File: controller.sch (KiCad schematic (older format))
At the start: 18 parts, among them P1 CONN_2, P2 CONN_2, P3 CONN_2, Q1 Q_NPN_EBC, SW1 SWITCH_INV, U1 LTC6992_TSOT_32_6, U2 POLOLU_3V3

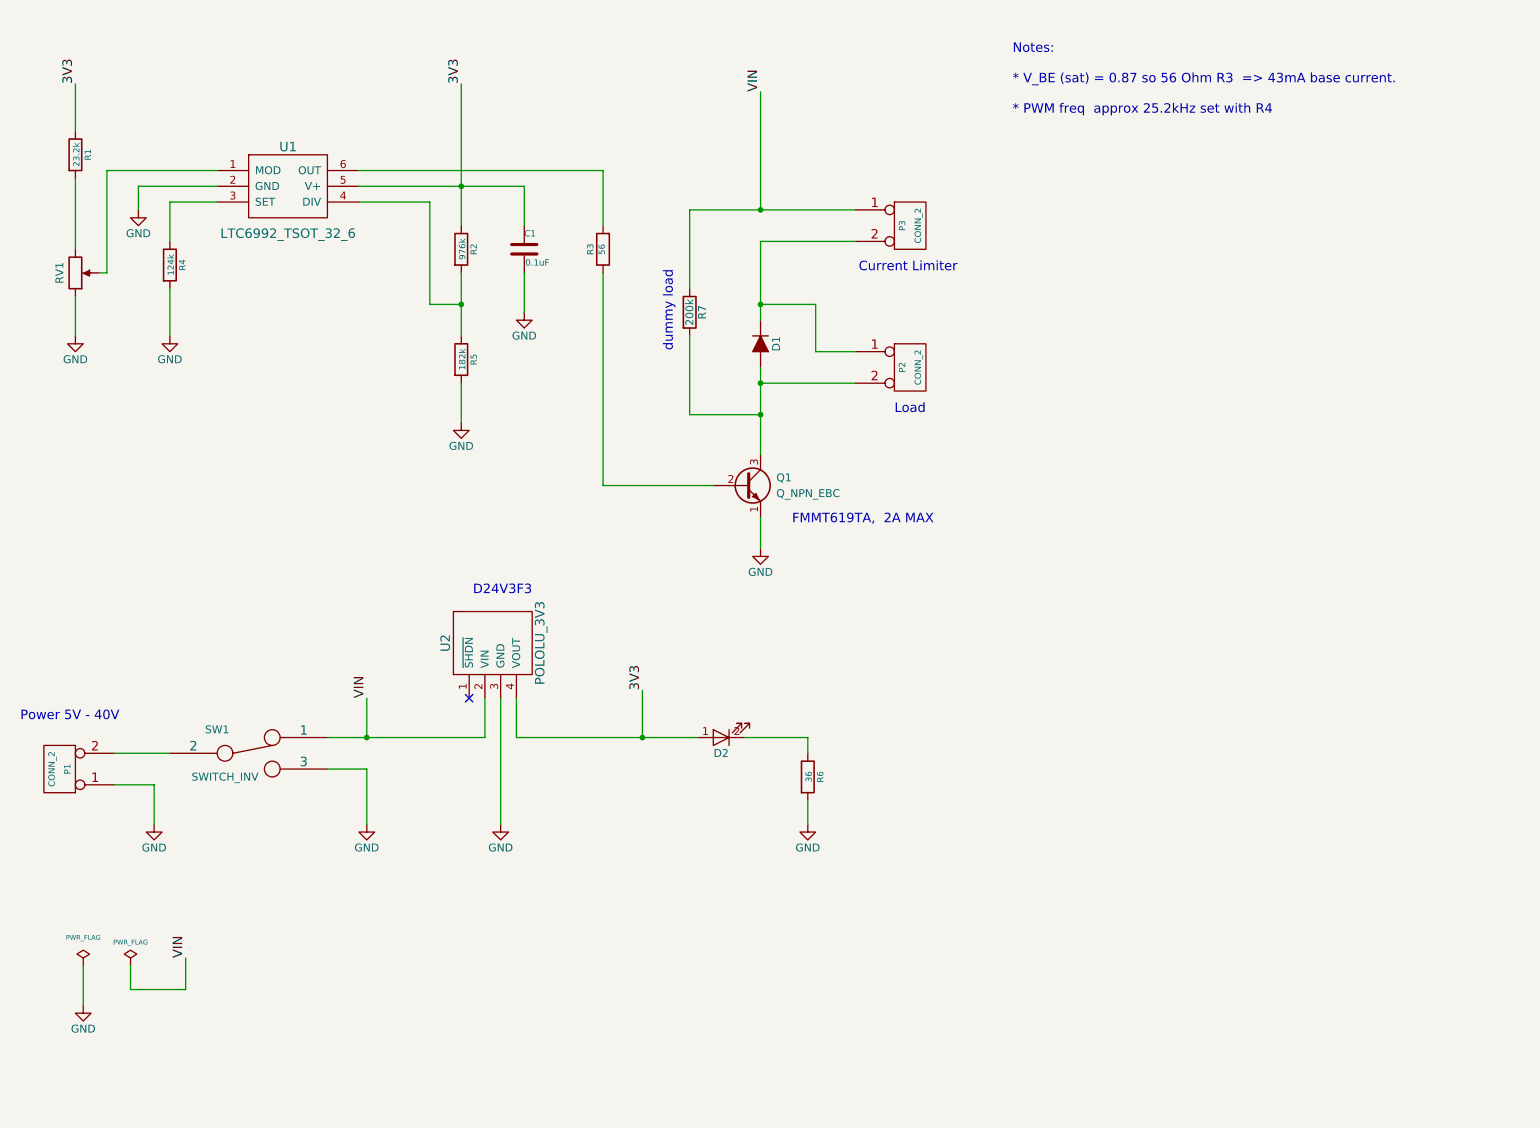
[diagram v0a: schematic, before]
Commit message: Modified to add external 0-1V analog input control. Made .zip archive of gerber files.
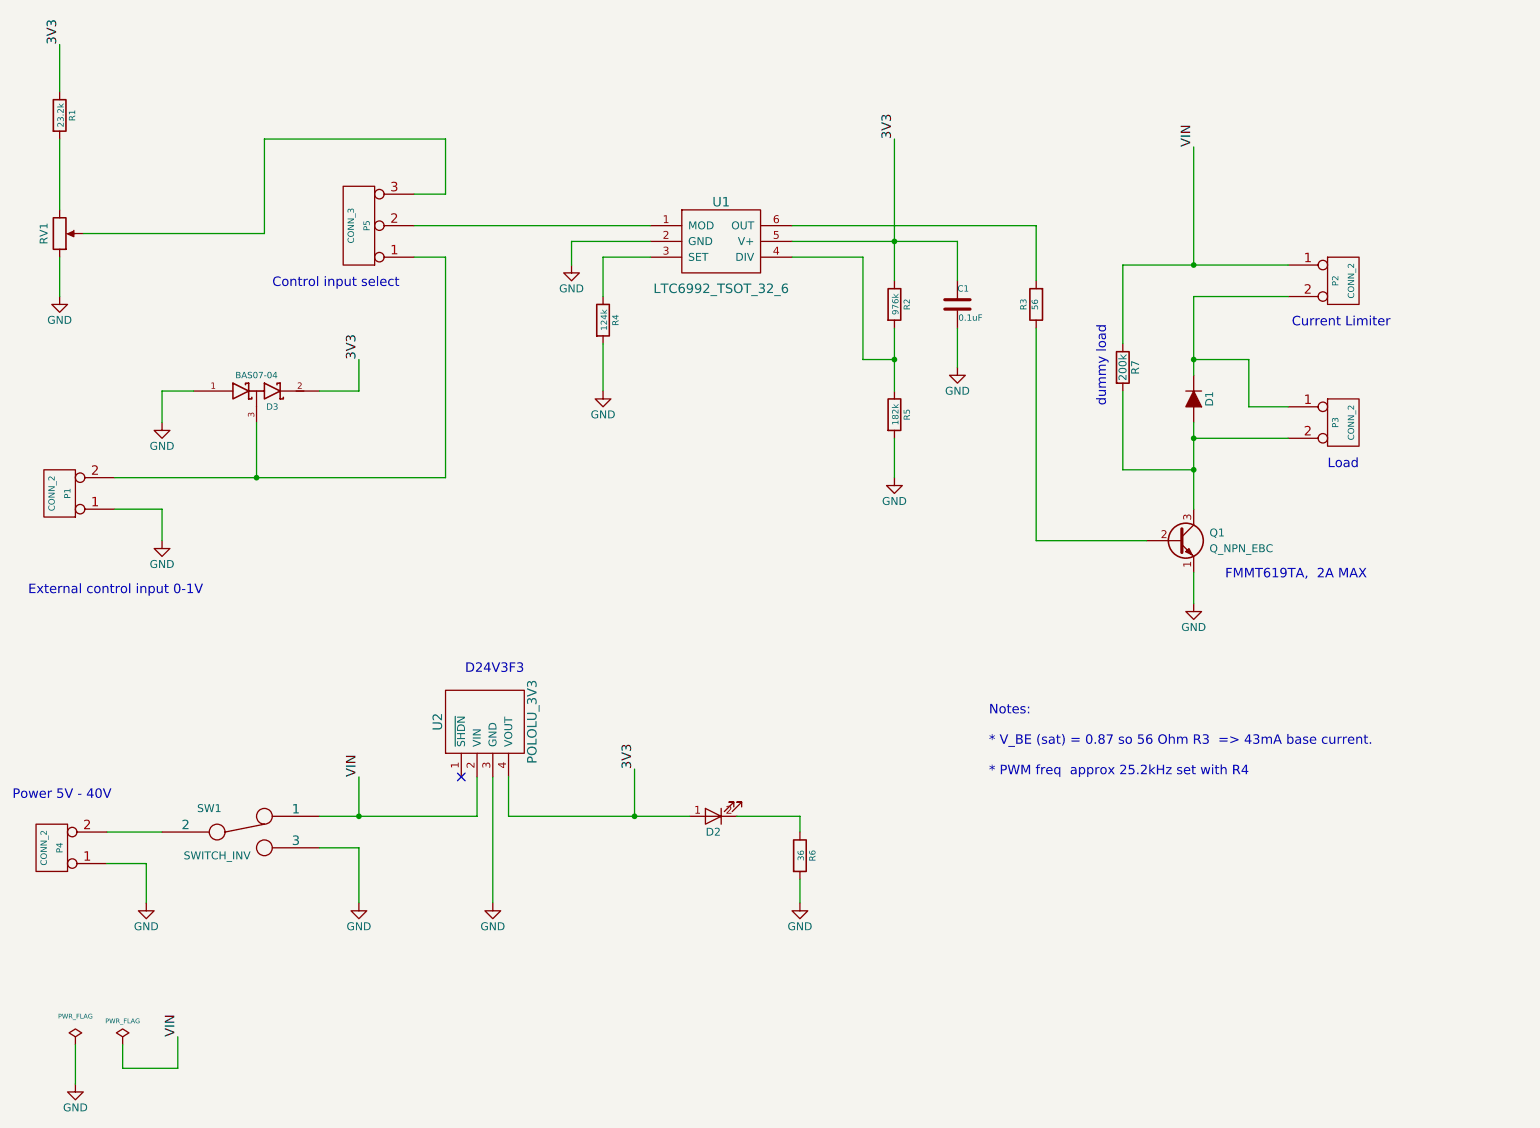
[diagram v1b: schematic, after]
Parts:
- added D3: BAS07-04, BAS07:SOT23EBC, symbol BAS07-04
- added P1: CONN_2, BLOCK_CONN_2:BLOCK_CONN_2X1, symbol CONN_2
- added P5: CONN_3, PIN_ARRAY_1X3:PIN_ARRAY_1X3, symbol CONN_3
- renumbered P3 to P2, P2 to P3, P1 to P4
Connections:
- net 3V3: now also D3.2 (cathode)
- net GND: now also D3.1 (Anode), P1.1 (P1)
- net at U1.1 (MOD): now also P5.2 (PM); no longer RV1.2
- new net: P5.3, RV1.2
- new net: D3.3 (AK), P1.2 (PM), P5.1 (P1)
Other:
- note added: "Control input select"
- note added: "External control input 0-1V"
- moved on the sheet: C1, D1, D2, P2, P3, P4, Q1, R1, R2, R3, R4, R5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
